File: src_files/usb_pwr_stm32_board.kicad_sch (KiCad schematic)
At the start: 20 parts

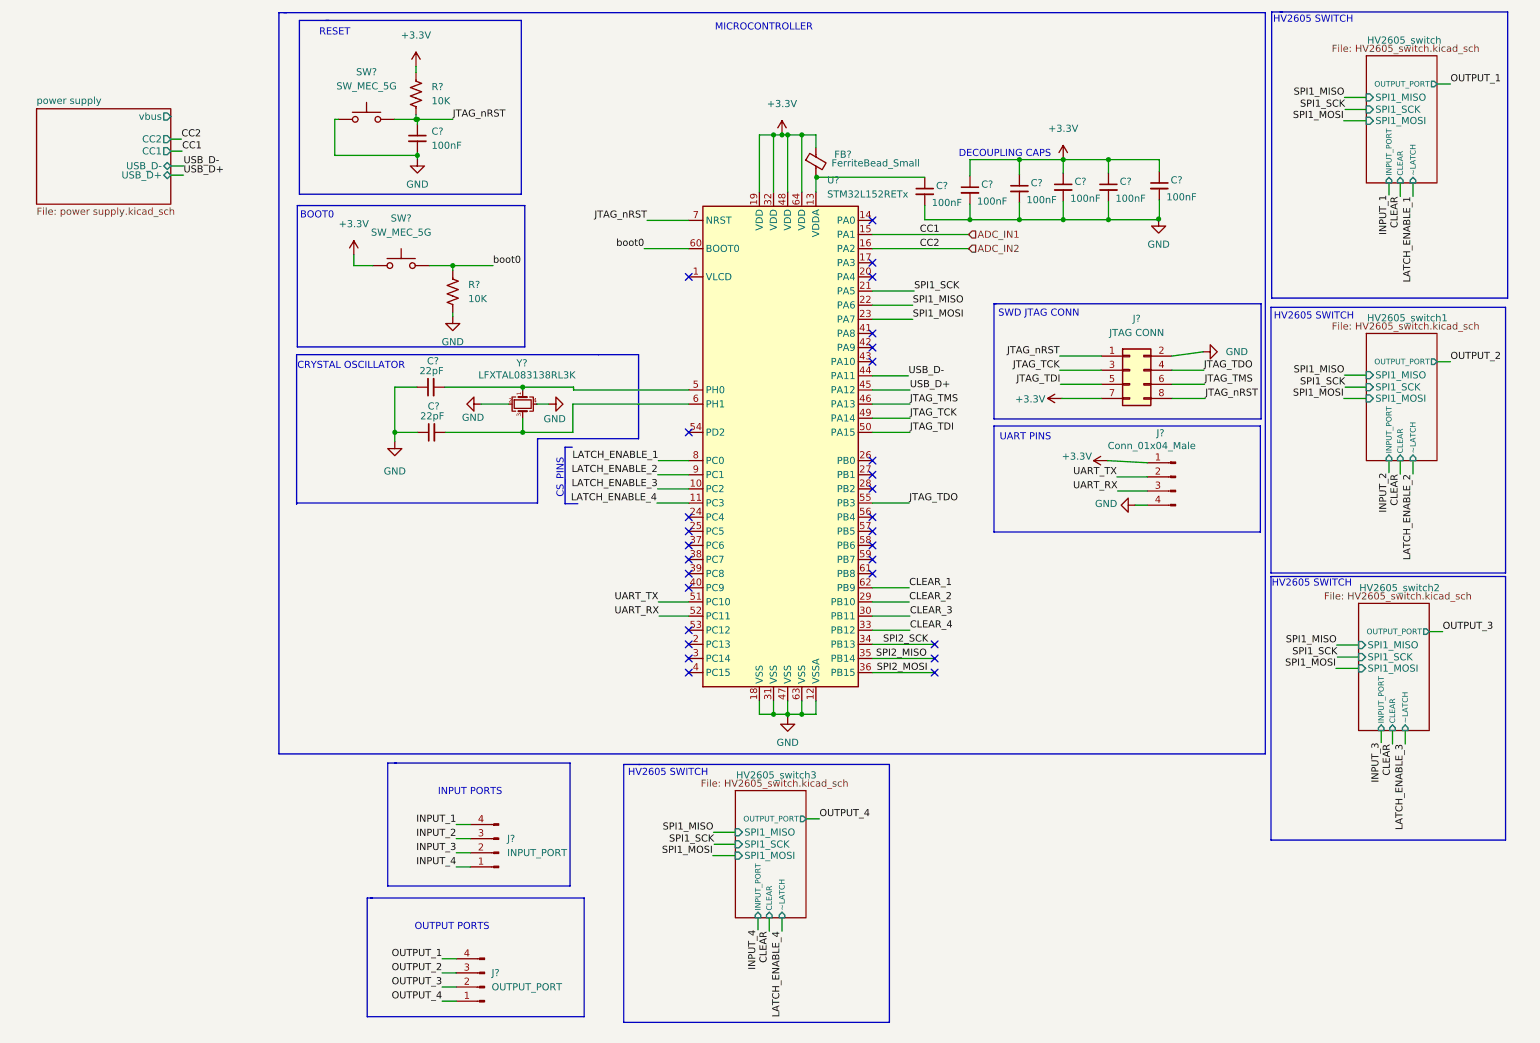
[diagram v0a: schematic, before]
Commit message: updated footprint assignment
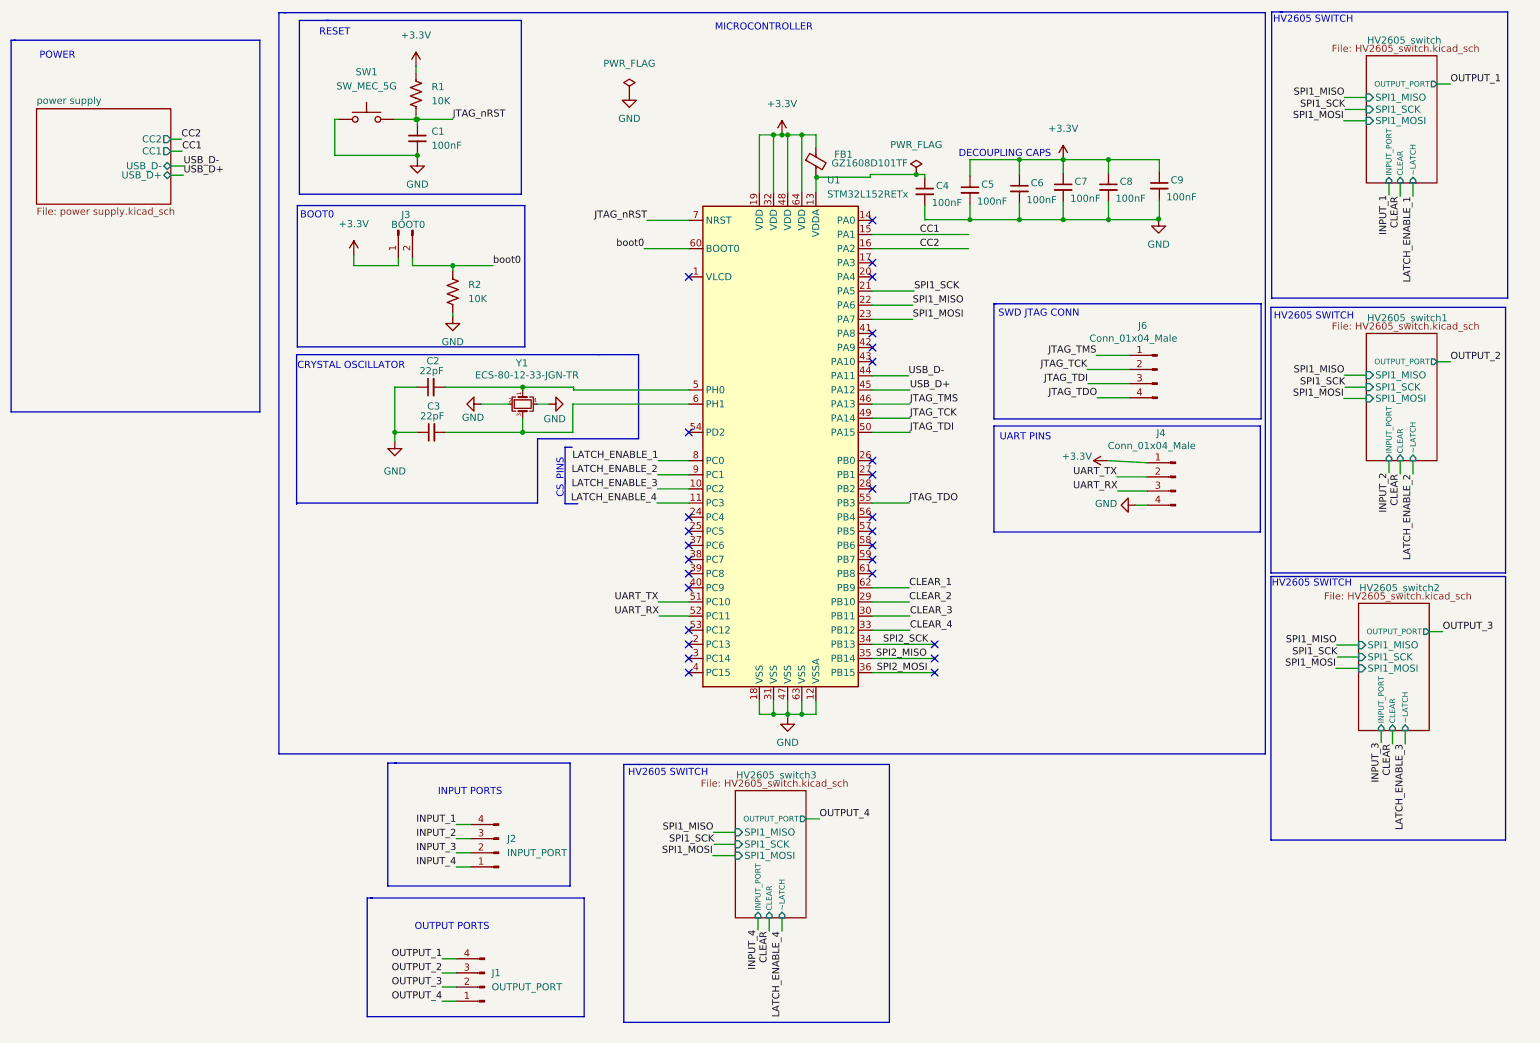
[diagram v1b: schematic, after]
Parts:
- removed J?: JTAG CONN, symbol Connector_Generic:Conn_02x04_Odd_Even
- removed SW?: SW_MEC_5G, symbol Switch:SW_MEC_5G
- added J3: BOOT0, Connector_PinHeader_2.54mm:PinHeader_1x02_P2.54mm_Vertical, symbol Connector:Conn_01x02_Male
- added J6: Conn_01x04_Male, Connector_PinHeader_2.54mm:PinHeader_1x04_P2.54mm_Vertical, symbol Connector:Conn_01x04_Male
- C1, C2, C3, C4, C5, C6, C7, C8, C9: renamed from C?; footprint (none) -> Capacitor_SMD:C_0603_1608Metric_Pad1.08x0.95mm_HandSolder
- FB1: renamed from FB?; value FerriteBead_Small -> GZ1608D101TF; footprint (none) -> Inductor_SMD:L_0603_1608Metric_Pad1.05x0.95mm_HandSolder
- J1, J2, J4: renamed from J?; footprint (none) -> Connector_PinHeader_2.54mm:PinHeader_1x04_P2.54mm_Vertical
- R1, R2: renamed from R?; footprint (none) -> Resistor_SMD:R_0603_1608Metric_Pad0.98x0.95mm_HandSolder
- SW1: renamed from SW?; footprint (none) -> greencharge-footprints:K2-1187SQ-D4SW-06
- Y1: renamed from Y?; value LFXTAL083138RL3K -> ECS-80-12-33-JGN-TR; footprint (none) -> Crystal:Crystal_SMD_3225-4Pin_3.2x2.5mm_HandSoldering
- gave numbers to parts that had none: 1
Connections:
- net +3V3: now also J3.1 (Pin_1)
- net JTAG_TCK: now also J6.2 (Pin_2)
- net JTAG_TDI: now also J6.3 (Pin_3)
- net JTAG_TDO: now also J6.4 (Pin_4)
- net JTAG_TMS: now also J6.1 (Pin_1)
- net boot0: now also J3.2 (Pin_2)
- net ADC_IN1 renamed CC1
- net ADC_IN2 renamed CC2
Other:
- sheet power supply ports: added none; removed vbus
- note added: "POWER"
